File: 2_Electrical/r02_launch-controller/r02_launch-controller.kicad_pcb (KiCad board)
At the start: 2 copper layers, 46.5 x 71.5 mm, 30 parts, among them J1 1729128, J2 XT30PW-M, J3 B2B-XH-AM, Q1 ZTX718, Q2 AOD413A, SW2 B2B-XH-AM, SW3 B2B-XH-AM, SW4 B2B-XH-AM

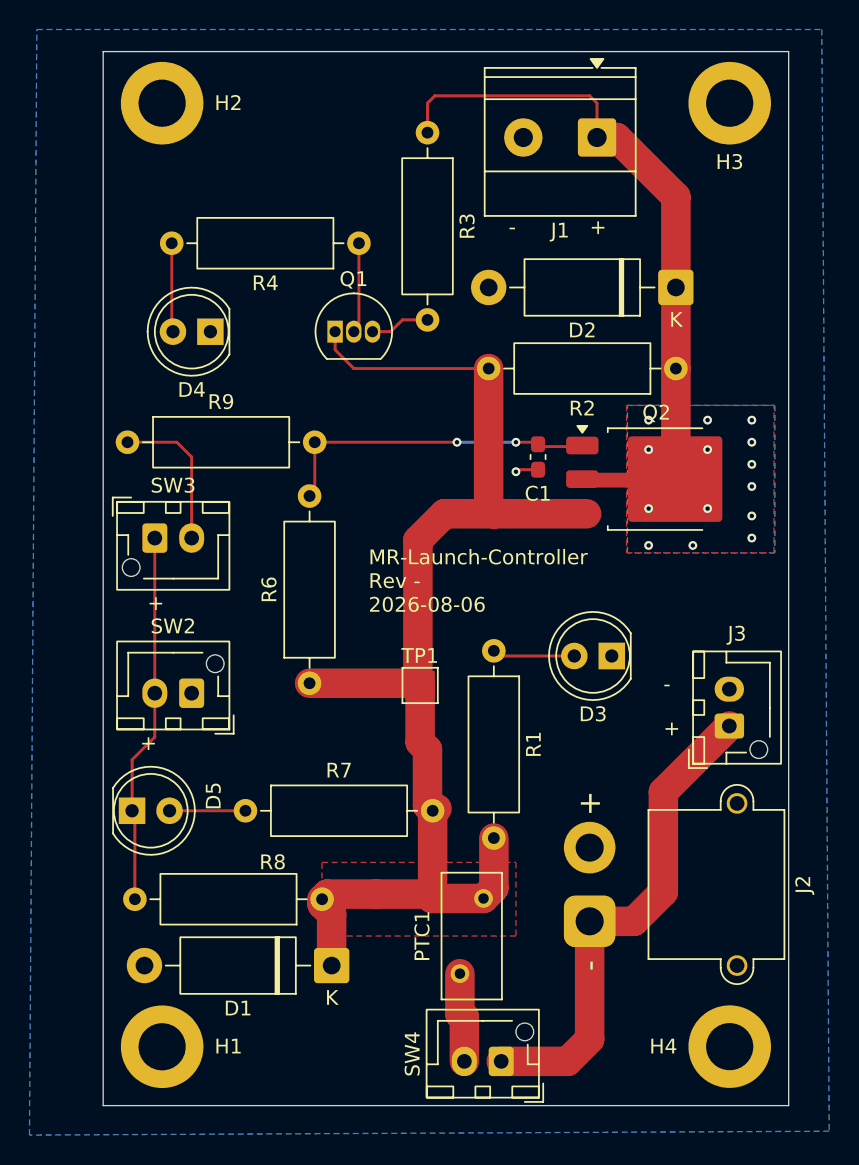
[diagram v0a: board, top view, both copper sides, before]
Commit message: layout: Laid out Rev A
Should be ready for a prototype. Same form factor as before, but all surface mount now.
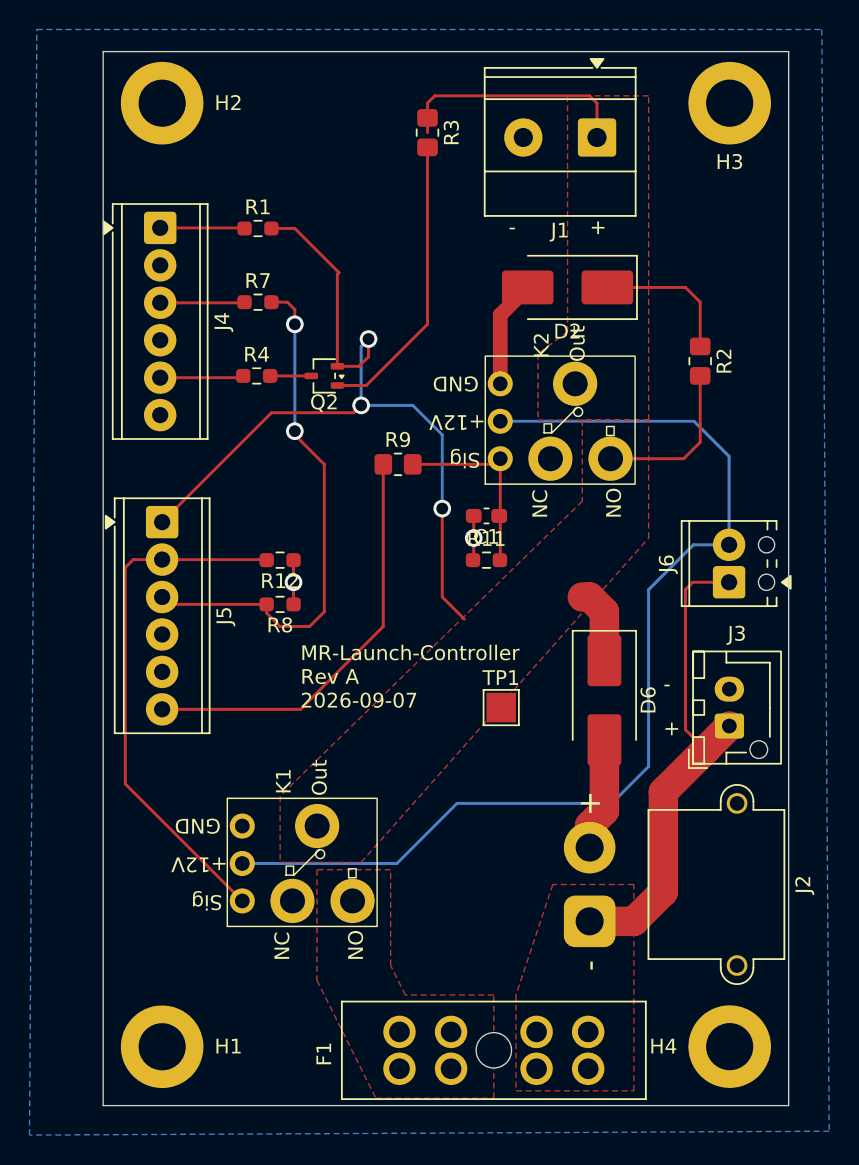
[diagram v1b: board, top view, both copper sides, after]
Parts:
- removed D1: P6KE7.5A/B, Diode_THT:D_DO-15_P12.70mm_Horizontal
- removed D3, D4, D5: LED, LED_THT:LED_D5.0mm
- removed PTC1: 0ZRG0250FF1E, Fuse:Fuse_BelFuse_0ZRE0012FF_L8.3mm_W3.8mm
- removed Q1: ZTX718, Package_TO_SOT_THT:TO-92_Inline
- removed R6: 4.7K, Resistor_THT:R_Axial_DIN0309_L9.0mm_D3.2mm_P12.70mm_Horizontal
- removed REF**: OSHW-Logo2_7.3x6mm_SilkScreen, Symbol:OSHW-Logo2_7.3x6mm_SilkScreen
- removed SW2, SW3, SW4: B2B-XH-AM, Connector_JST:JST_XH_B2B-XH-AM_1x02_P2.50mm_Vertical
- added D6: SM6T18A, Diode_SMD:D_SMB_Handsoldering, F.Cu at (132.5, 117.5)
- added F1: 178.6165.0001, Fuse:FuseHolder_Blade_ATO_Littelfuse_FLR_178.6165, F.Cu at (131.4, 142.5)
- added J4: 1725698, TerminalBlock_Phoenix:TerminalBlock_Phoenix_MPT-0,5-6-2.54_1x06_P2.54mm_Horizontal, F.Cu at (102.4, 85.5)
- added J5: 1725698, TerminalBlock_Phoenix:TerminalBlock_Phoenix_MPT-0,5-6-2.54_1x06_P2.54mm_Horizontal, F.Cu at (102.5, 105.4)
- added J6: Screw_Terminal_01x02, TerminalBlock_Phoenix:TerminalBlock_Phoenix_MPT-0,5-2-2.54_1x02_P2.54mm_Horizontal, F.Cu at (141.0, 109.5)
- added K1: ~, JM-Library:12V-relay, F.Cu at (107.9, 131.1)
- added K2: ~, JM-Library:12V-relay, F.Cu at (125.4, 101.1)
- added R11: 10K, Resistor_SMD:R_0603_1608Metric_Pad0.98x0.95mm_HandSolder, F.Cu at (124.5, 108.0)
- added R12: 10K, Resistor_SMD:R_0603_1608Metric_Pad0.98x0.95mm_HandSolder, F.Cu at (110.5, 108.0)
- D2: value P6KE7.5A/B -> SM6T18A; footprint Diode_THT:D_DO-15_P12.70mm_Horizontal -> Diode_SMD:D_SMB_Handsoldering
- Q2: value AOD413A -> BC807W; footprint Package_TO_SOT_SMD:TO-252-3_TabPin2 -> Package_TO_SOT_SMD:SOT-323_SC-70
- R1, R4, R7, R8: footprint Resistor_THT:R_Axial_DIN0309_L9.0mm_D3.2mm_P12.70mm_Horizontal -> Resistor_SMD:R_0603_1608Metric_Pad0.98x0.95mm_HandSolder
- R2, R3, R9: footprint Resistor_THT:R_Axial_DIN0309_L9.0mm_D3.2mm_P12.70mm_Horizontal -> Resistor_SMD:R_0805_2012Metric_Pad1.20x1.40mm_HandSolder
- moved G*** 64.0 mm to (110.0, 77.5)
- moved R7 34.5 mm to (109.0, 90.5)
- moved R1 32.8 mm to (109.0, 85.5), turned to 0 degrees
- moved Q2 23.6 mm to (113.5, 95.5), turned to 180 degrees
- moved R8 20.2 mm to (110.5, 111.0)
- moved R9 18.4 mm to (118.5, 101.5)
- moved R4 11.4 mm to (108.9, 95.5), turned to 0 degrees
- moved D2 7.35 mm to (130.0, 89.5)
- moved TP1 5.70 mm to (125.5, 118.0)
- moved C1 5.32 mm to (124.5, 105.0), turned to 180 degrees
- moved R2 1.72 mm to (139.0, 94.5), turned to -90 degrees
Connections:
- C1 pad 1: /launch -> /launch_sw
- Q2 pad 1: /launch -> Net-(Q2-B)
- Q2 pad 2: /igniter_hot -> /safed_power
- Q2 pad 3: /safed_power -> Net-(Q2-C)
- R1 pad 1: Net-(D3-A) -> /power_LED
- R3 pad 2: Net-(Q1-B) -> Net-(Q2-B)
- R4 pad 1: Net-(Q1-C) -> /continuity_LED
- R4 pad 2: Net-(D4-A) -> Net-(Q2-C)
- R7 pad 1: Net-(D5-A) -> /armed_LED
- R7 pad 2: /safed_power -> /armed
- R8 pad 1: /safed_power -> GND
- R8 pad 2: /arm -> /armed
- R9 pad 1: Net-(SW3-B) -> /launch
- R9 pad 2: /launch -> /launch_sw
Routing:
- net +12V: track 0.00 -> 71.5 mm
- net /safe_relay: track 0.00 -> 35.7 mm
- net /armed: track 0.00 -> 35.7 mm, vias 0 -> 2
- net /arm: track 25.2 -> 0.00 mm
- net /igniter_hot: track 49.7 -> 26.0 mm, vias 14 -> 0
- net GND: track 1.56 -> 22.5 mm, vias 1 -> 2
- net Net-(Q2-B): track 0.00 -> 19.8 mm
- net /launch_sw: track 0.00 -> 13.0 mm
- net /safed_power: track 85.9 -> 73.0 mm, vias 0 -> 3
- net Net-(SW3-B): track 10.3 -> 0.00 mm
- net Net-(SW4-B): track 7.06 -> 0.00 mm
- net Net-(Q1-C): track 6.14 -> 0.00 mm
- net Net-(D4-A): track 6.04 -> 0.00 mm
- net /power_LED: track 0.00 -> 5.74 mm
- net /armed_LED: track 0.00 -> 5.74 mm
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- added copper zone on F.Cu, net /battery
- added copper zone on F.Cu, net Net-(K1-NO)
- removed copper zone on B.Cu, net /igniter_hot
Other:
- board text added: "MR-Launch-Controller Rev A 2026-09-07"
- board text removed: "MR-Launch-Controller Rev - 2026-08-06"
